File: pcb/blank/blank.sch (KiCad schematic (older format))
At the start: 2 parts

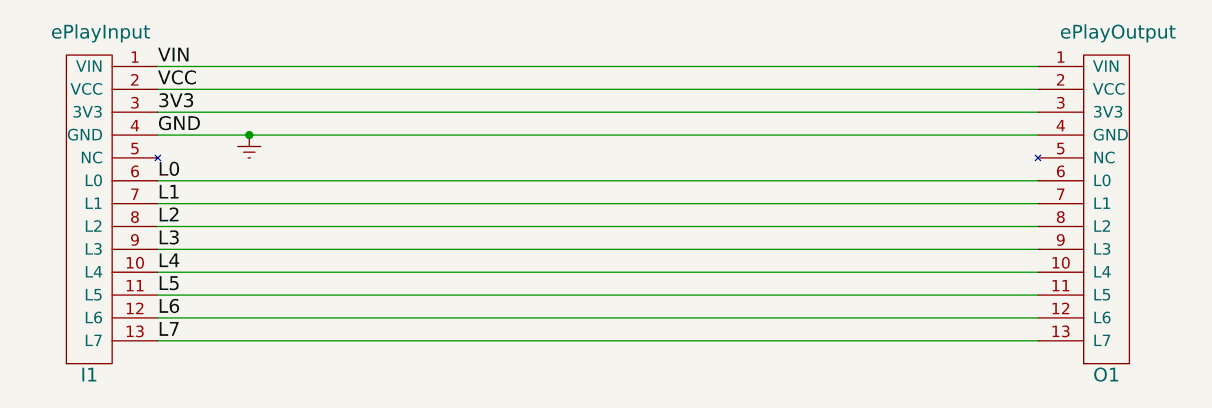
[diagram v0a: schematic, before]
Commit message: Added a new "power" and LEDs module (split into two half size modules)
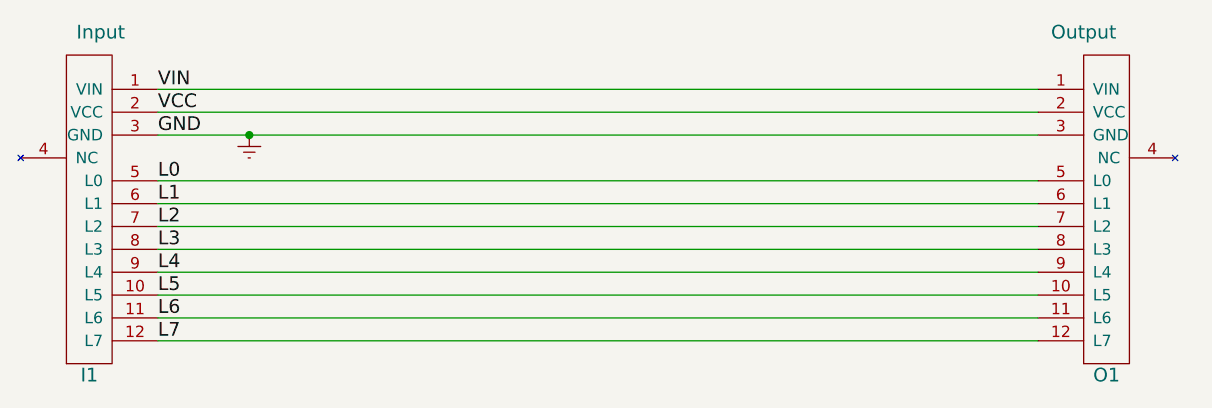
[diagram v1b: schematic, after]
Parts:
- removed I1: ePlayInput, Pin_Headers:Pin_Header_Straight_1x13_Pitch2.54mm, symbol ePlayInput
- removed O1: ePlayOutput, Socket_Strips:Socket_Strip_Straight_1x13_Pitch2.54mm, symbol ePlayOutput
- added I1: Input, Pin_Headers:Pin_Header_Straight_1x12_Pitch2.54mm, symbol Input
- added O1: Output, Socket_Strips:Socket_Strip_Straight_1x12_Pitch2.54mm, symbol Output
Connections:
- net Earth: now also I1.3 (GND), O1.3 (GND)
- net L0: now also I1.5 (L0), O1.5 (L0)
- net L1: now also I1.6 (L1), O1.6 (L1)
- net L2: now also I1.7 (L2), O1.7 (L2)
- net L3: now also I1.8 (L3), O1.8 (L3)
- net L4: now also I1.9 (L4), O1.9 (L4)
- net L5: now also I1.10 (L5), O1.10 (L5)
- net L6: now also I1.11 (L6), O1.11 (L6)
- net L7: now also I1.12 (L7), O1.12 (L7)
- net VCC: now also I1.2 (VCC), O1.2 (VCC)
- net VIN: now also I1.1 (VIN), O1.1 (VIN)
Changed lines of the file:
@@
 EESchema Schematic File Version 2
+LIBS:blank-rescue
 LIBS:power
 LIBS:device
@@
 LIBS:eplay
 LIBS:Switch
-LIBS:buttons-cache
+LIBS:blank-cache
 EELAYER 25 0
 EELAYER END
@@
 Comment4 ""
 $EndDescr
-$Comp
-L ePlayInput I1
-U 1 1 5AC243A7
-P 1950 1600
-F 0 "I1" H 1950 50  60  0000 C CNN
-F 1 "ePlayInput" H 2000 1550 60  0000 C CNN
-F 2 "Pin_Headers:Pin_Header_Straight_1x13_Pitch2.54mm" H 2000 1550 60  0001 C CNN
-F 3 "" H 2000 1550 60  0001 C CNN
-	1    1950 1600
-	1    0    0    -1
-$EndComp
-$Comp
-L ePlayOutput O1
-U 1 1 5AC241F8
-P 6400 1600
-F 0 "O1" H 6400 50  60  0000 C CNN
-F 1 "ePlayOutput" H 6450 1550 60  0000 C CNN
-F 2 "Socket_Strips:Socket_Strip_Straight_1x13_Pitch2.54mm" H 6450 1550 60  0001 C CNN
-F 3 "" H 6450 1550 60  0001 C CNN
-	1    6400 1600
-	1    0    0    -1
-$EndComp
-Wire Wire Line
-	2250 1800 6100 1800
 Wire Wire Line
 	2250 1900 6100 1900
@@
 GND
 Text Label 2250 2000 0    60   ~ 0
-3V3
+VCC
 Text Label 2250 1900 0    60   ~ 0
-VCC
-Text Label 2250 1800 0    60   ~ 0
 VIN
 Text Label 2250 2300 0    60   ~ 0
@@
 $EndComp
 Connection ~ 2650 2100
+$Comp
+L Input I1
+U 1 1 5AC3D559
+P 1950 1600
+F 0 "I1" H 1950 50  60  0000 C CNN
+F 1 "Input" H 2000 1550 60  0000 C CNN
+F 2 "Pin_Headers:Pin_Header_Straight_1x12_Pitch2.54mm" H 2000 1550 60  0001 C CNN
+F 3 "" H 2000 1550 60  0001 C CNN
+	1    1950 1600
+	1    0    0    -1
+$EndComp
+$Comp
+L Output O1
+U 1 1 5AC3D61D
+P 6400 1600
+F 0 "O1" H 6400 50  60  0000 C CNN
+F 1 "Output" H 6300 1550 60  0000 C CNN
+F 2 "Socket_Strips:Socket_Strip_Straight_1x12_Pitch2.54mm" H 6450 1550 60  0001 C CNN
+F 3 "" H 6450 1550 60  0001 C CNN
+	1    6400 1600
+	1    0    0    -1
+$EndComp
 $EndSCHEMATC

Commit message: Tidied up blank, and removed the voltage regulator from "power" module.
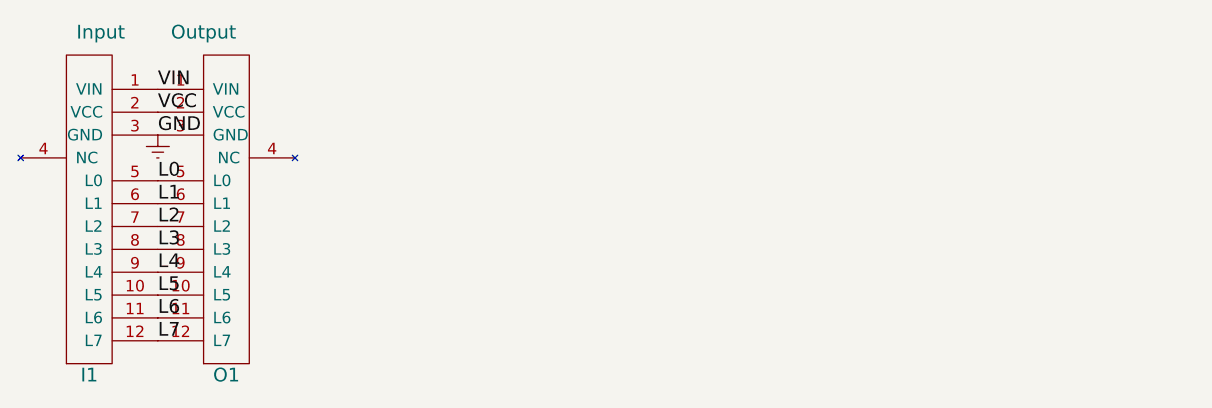
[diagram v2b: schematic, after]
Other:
- moved on the sheet: O1
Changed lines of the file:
@@
 Comment4 ""
 $EndDescr
-Wire Wire Line
-	2250 1900 6100 1900
-Wire Wire Line
-	2250 2000 6100 2000
-Wire Wire Line
-	2250 2100 6100 2100
-Wire Wire Line
-	2250 2300 6100 2300
-Wire Wire Line
-	2250 2400 6100 2400
-Wire Wire Line
-	2250 2500 6100 2500
-Wire Wire Line
-	2250 2600 6100 2600
-Wire Wire Line
-	2250 2700 6100 2700
-Wire Wire Line
-	2250 2800 6100 2800
-Wire Wire Line
-	2250 2900 6100 2900
-Wire Wire Line
-	2250 3000 6100 3000
 Text Label 2250 2100 0    60   ~ 0
 GND
@@
 L Earth #PWR01
 U 1 1 5AC24527
-P 2650 2100
-F 0 "#PWR01" H 2650 1850 50  0001 C CNN
-F 1 "Earth" H 2650 1950 50  0001 C CNN
-F 2 "" H 2650 2100 50  0001 C CNN
-F 3 "" H 2650 2100 50  0001 C CNN
-	1    2650 2100
+P 2250 2100
+F 0 "#PWR01" H 2250 1850 50  0001 C CNN
+F 1 "Earth" H 2250 1950 50  0001 C CNN
+F 2 "" H 2250 2100 50  0001 C CNN
+F 3 "" H 2250 2100 50  0001 C CNN
+	1    2250 2100
 	1    0    0    -1
 $EndComp
-Connection ~ 2650 2100
 $Comp
 L Input I1
@@
 L Output O1
 U 1 1 5AC3D61D
-P 6400 1600
-F 0 "O1" H 6400 50  60  0000 C CNN
-F 1 "Output" H 6300 1550 60  0000 C CNN
-F 2 "Socket_Strips:Socket_Strip_Straight_1x12_Pitch2.54mm" H 6450 1550 60  0001 C CNN
-F 3 "" H 6450 1550 60  0001 C CNN
-	1    6400 1600
+P 2550 1600
+F 0 "O1" H 2550 50  60  0000 C CNN
+F 1 "Output" H 2450 1550 60  0000 C CNN
+F 2 "Socket_Strips:Socket_Strip_Straight_1x12_Pitch2.54mm" H 2600 1550 60  0001 C CNN
+F 3 "" H 2600 1550 60  0001 C CNN
+	1    2550 1600
 	1    0    0    -1
 $EndComp
